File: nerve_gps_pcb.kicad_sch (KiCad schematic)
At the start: 20 parts, among them J1 BF080-16-A-1-L-C, J2 WS2812B, J3 5V GPIO Breakout, U1 SAM-M10Q, U2 TXB0104QPWRQ1

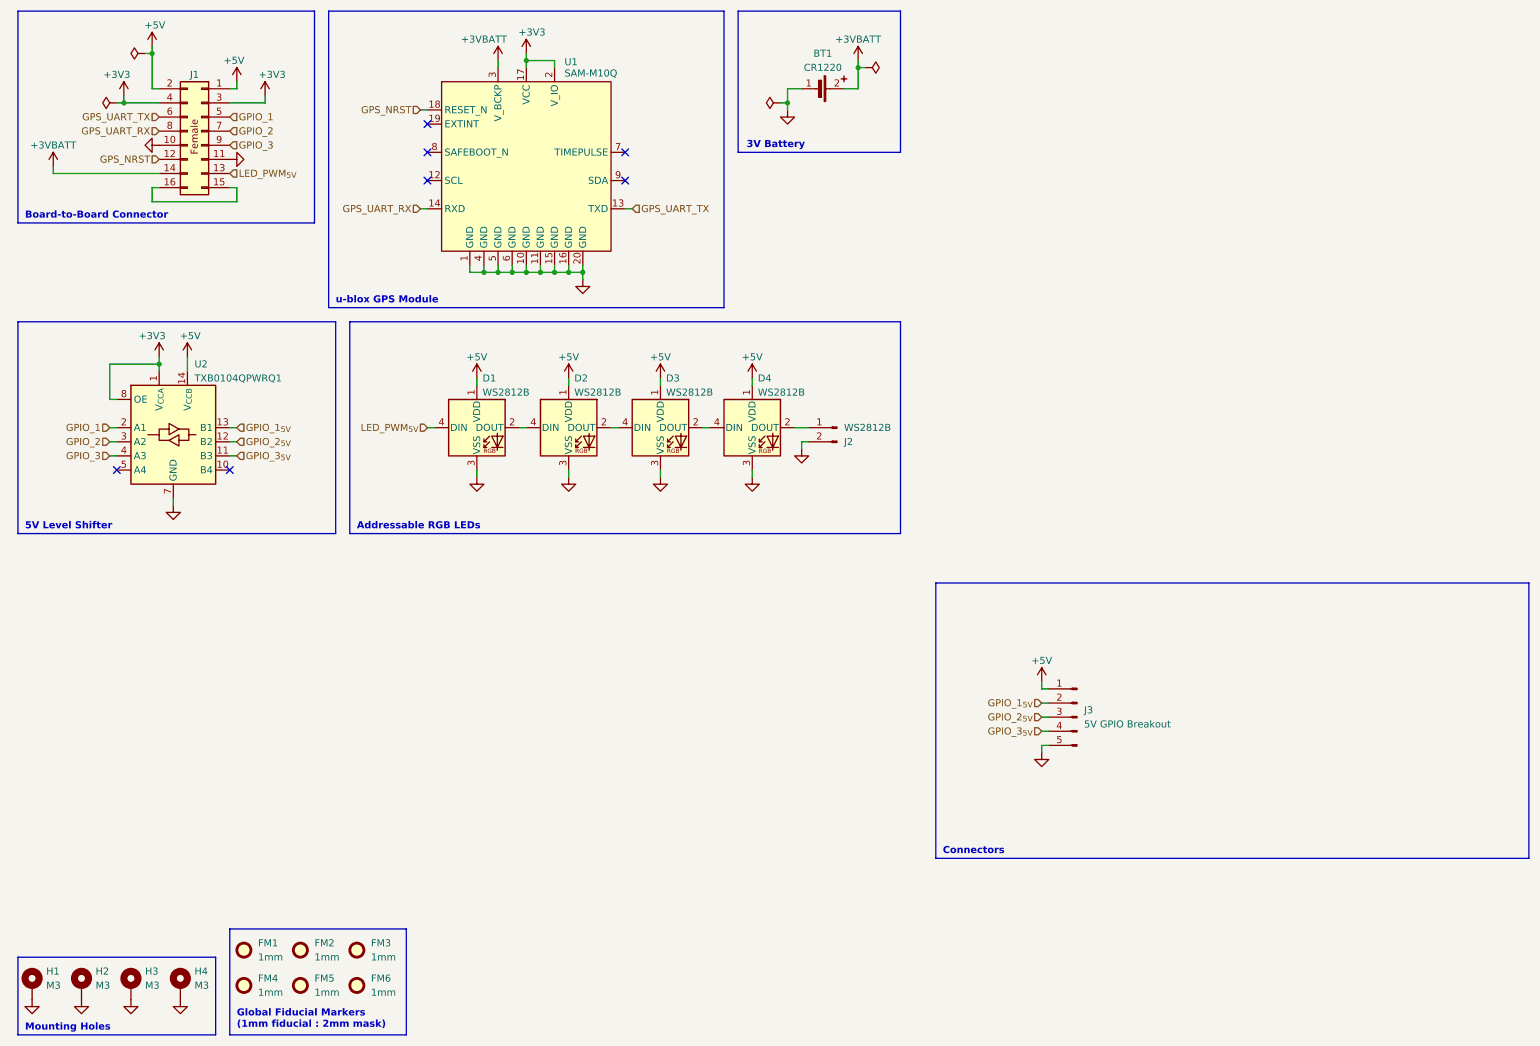
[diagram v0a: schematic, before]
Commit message: Add minor decoupling caps
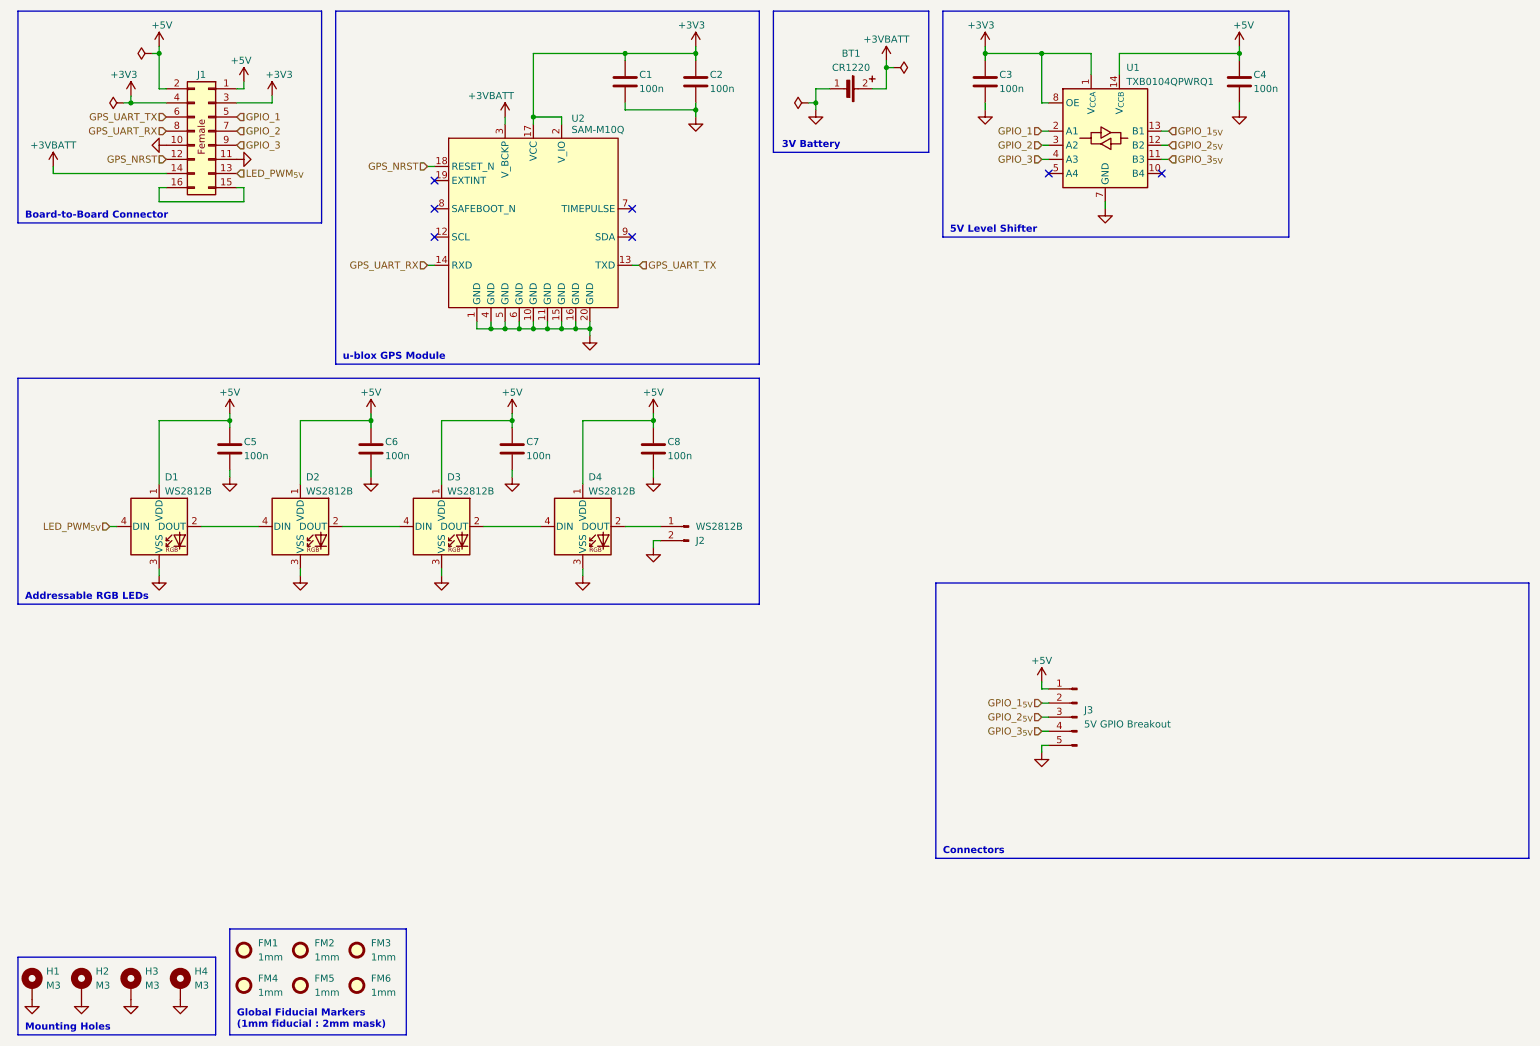
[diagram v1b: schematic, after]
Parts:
- added C1, C2, C3, C4, C5, C6, C7, C8: 100n, Capacitor_SMD:C_0603_1608Metric, symbol Device:C
- renumbered U2 to U1, U1 to U2
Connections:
- net +3V3: now also C1.1, C2.1, C3.1
- net +5V: now also C4.1, C5.1, C6.1, C7.1, C8.1
- net GND: now also C1.2, C2.2, C3.2, C4.2, C5.2, C6.2, C7.2, C8.2
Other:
- moved on the sheet: BT1, D1, D2, D3, D4, J1, J2, U1, U2

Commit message: Add CR1220 reverse polarity schottky diode
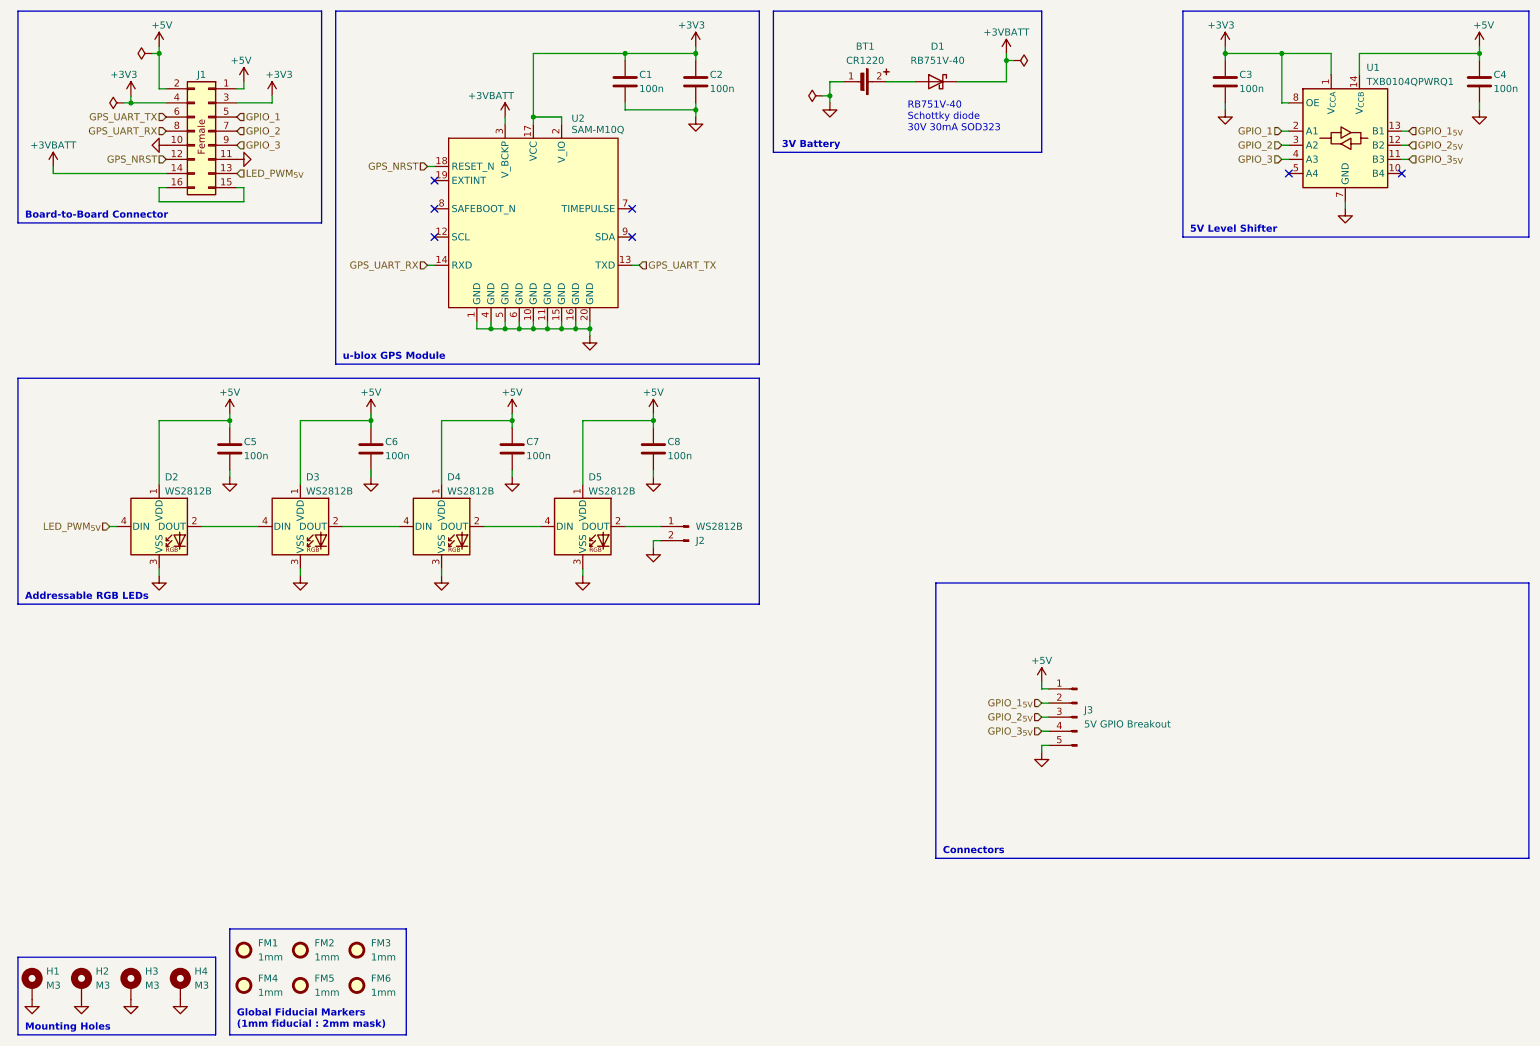
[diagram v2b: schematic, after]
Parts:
- added D1: RB751V-40, Diode_SMD:D_SOD-323, symbol Device:D_Schottky
- renumbered D1 to D2, D2 to D3, D3 to D4, D4 to D5
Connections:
- net +3VBATT: now also D1.1 (K); no longer BT1.2
- new net: BT1.2, D1.2 (A)
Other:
- note added: "RB751V-40 Schottky diode 30V 30mA SOD323"
- moved on the sheet: BT1, C3, C4, U1

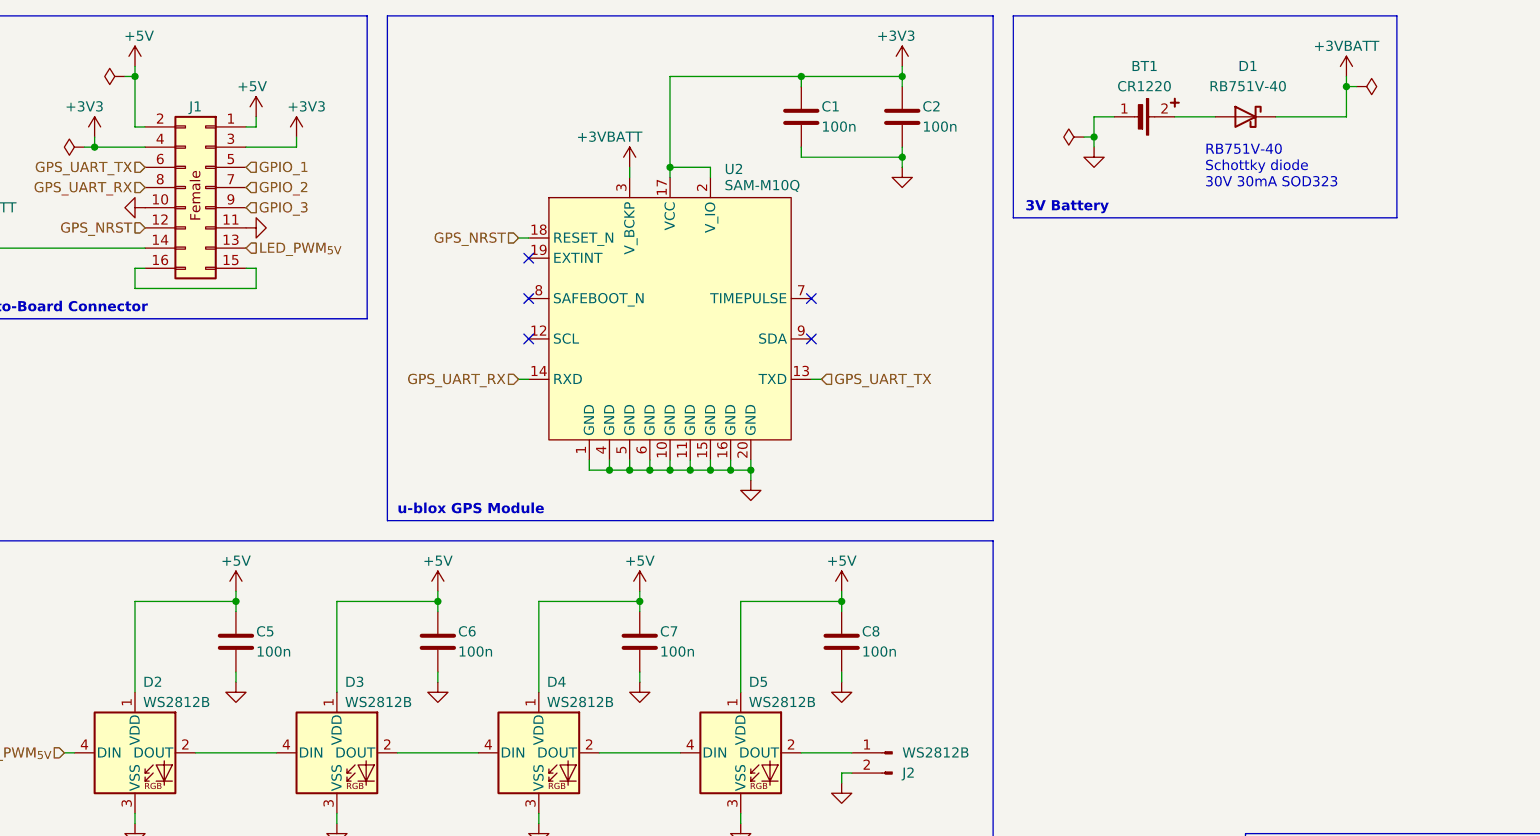
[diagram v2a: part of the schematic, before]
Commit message: Remove CR1220 schottky diode
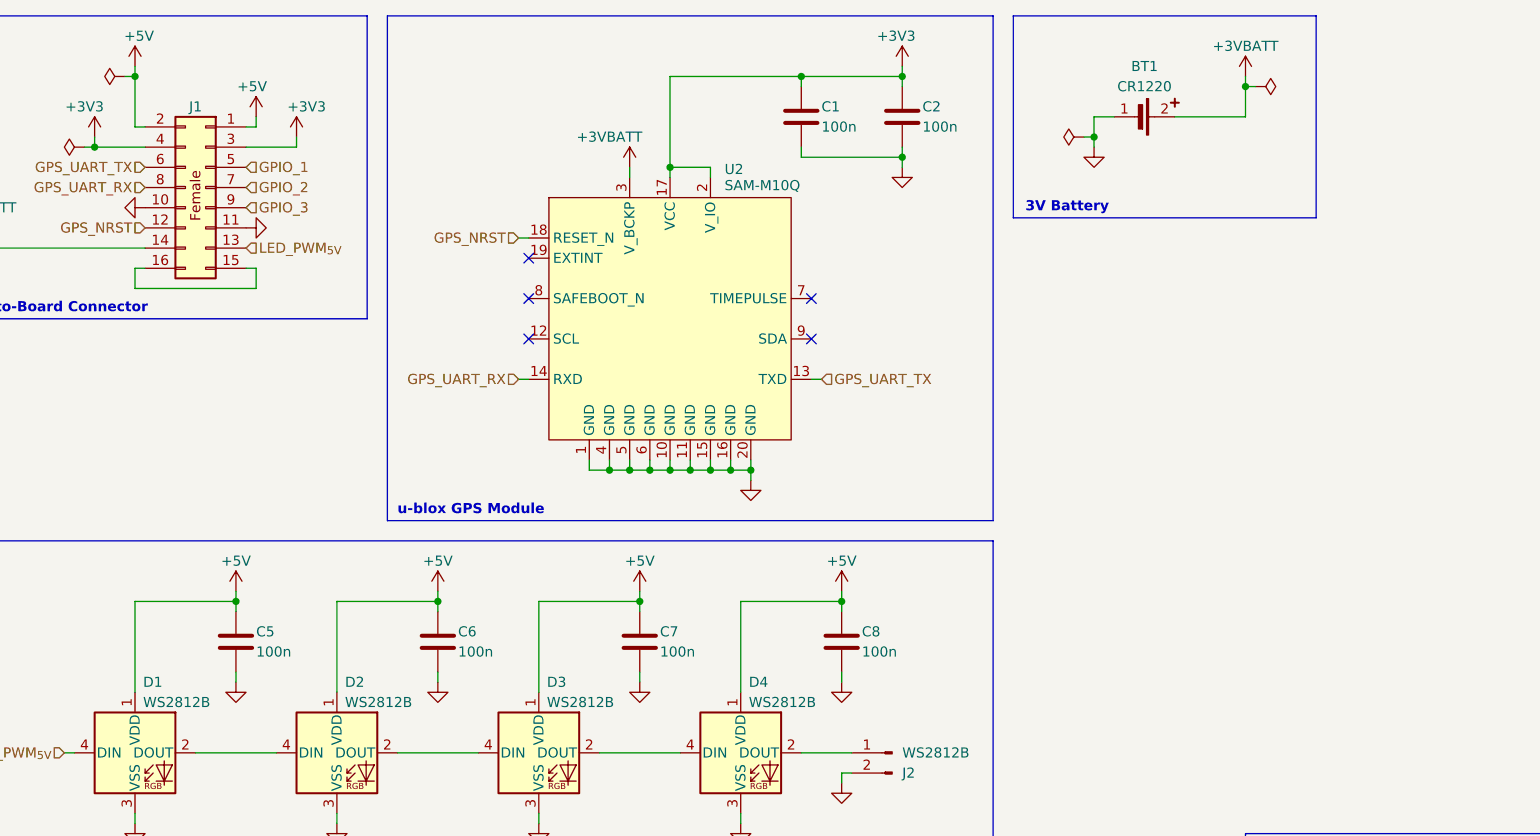
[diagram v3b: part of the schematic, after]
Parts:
- removed D1: RB751V-40, Diode_SMD:D_SOD-323, symbol Device:D_Schottky
- renumbered D2 to D1, D3 to D2, D4 to D3, D5 to D4
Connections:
- net +3VBATT: now also BT1.2
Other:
- note removed: "RB751V-40 Schottky diode 30V 30mA SOD323"
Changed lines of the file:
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@@
 	(rectangle
 		(start 148.59 12.7)
-		(end 196.85 38.1)
+		(end 186.69 38.1)
 		(stroke
 			(width 0)
@@
 		)
 	)
-	(text "RB751V-40\nSchottky diode\n30V 30mA SOD323"
-		(exclude_from_sim no)
-		(at 172.72 31.75 0)
-		(effects
-			(font
-				(size 1.27 1.27)
-				(thickness 0.1588)
-			)
-			(justify left)
-		)
-	)
 	(junction
 		(at 115.57 69.85)
@@
 	)
 	(junction
-		(at 190.5 21.59)
+		(at 177.8 21.59)
 		(diameter 0)
 		(color 0 0 0 0)
@@
 	(wire
 		(pts
-			(xy 190.5 20.32) (xy 190.5 21.59)
+			(xy 177.8 20.32) (xy 177.8 21.59)
 		)
 		(stroke
@@
 	(wire
 		(pts
-			(xy 181.61 25.4) (xy 190.5 25.4)
-		)
-		(stroke
-			(width 0)
-			(type default)
-		)
-	)
-	(wire
-		(pts
 			(xy 114.3 113.03) (xy 114.3 114.3)
 		)
@@
 	(wire
 		(pts
-			(xy 190.5 21.59) (xy 191.77 21.59)
+			(xy 177.8 21.59) (xy 179.07 21.59)
 		)
 		(stroke
@@
 	(wire
 		(pts
-			(xy 168.91 25.4) (xy 173.99 25.4)
+			(xy 168.91 25.4) (xy 177.8 25.4)
 		)
 		(stroke
@@
 	(wire
 		(pts
-			(xy 190.5 21.59) (xy 190.5 25.4)
+			(xy 177.8 21.59) (xy 177.8 25.4)
 		)
 		(stroke
@@
 		(on_board yes)
 		(dnp no)
-		(property "Reference" "D5"
+		(property "Reference" "D4"
 			(at 115.316 96.52 0)
 			(effects
@@
 			(project "nerve_gps_pcb"
 				(path "/c0277862-b3f2-4e0e-986f-34702f0543f0"
-					(reference "D5")
+					(reference "D4")
 					(unit 1)
 				)
@@
 	)
 	(symbol
-		(lib_id "Device:D_Schottky")
-		(at 177.8 25.4 0)
-		(mirror y)
-		(unit 1)
-		(exclude_from_sim no)
-		(in_bom yes)
-		(on_board yes)
-		(dnp no)
-		(property "Reference" "D1"
-			(at 178.1175 19.05 0)
-			(effects
-				(font
-					(size 1.27 1.27)
-				)
-			)
-		)
-		(property "Value" "RB751V-40"
-			(at 178.1175 21.59 0)
-			(effects
-				(font
-					(size 1.27 1.27)
-				)
-			)
-		)
-		(property "Footprint" "Diode_SMD:D_SOD-323"
-			(at 177.8 25.4 0)
-			(effects
-				(font
-					(size 1.27 1.27)
-				)
-				(hide yes)
-			)
-		)
-		(property "Datasheet" "~"
-			(at 177.8 25.4 0)
-			(effects
-				(font
-					(size 1.27 1.27)
-				)
-				(hide yes)
-			)
-		)
-		(property "Description" "Schottky diode"
-			(at 177.8 25.4 0)
-			(effects
-				(font
-					(size 1.27 1.27)
-				)
-				(hide yes)
-			)
-		)
-		(pin "1"
-		)
-		(pin "2"
-		)
-		(instances
-			(project "nerve_gps_pcb"
-				(path "/c0277862-b3f2-4e0e-986f-34702f0543f0"
-					(reference "D1")
-					(unit 1)
-				)
-			)
-		)
-	)
-	(symbol
 		(lib_id "power:GND")
 		(at 15.24 190.5 0)
@@
 	(symbol
 		(lib_id "power:+3V3")
-		(at 190.5 20.32 0)
+		(at 177.8 20.32 0)
 		(unit 1)
 		(exclude_from_sim no)
@@
 		(dnp no)
 		(property "Reference" "#PWR05"
-			(at 190.5 24.13 0)
+			(at 177.8 24.13 0)
 			(effects
 				(font
@@
 		)
 		(property "Value" "+3VBATT"
-			(at 190.5 16.51 0)
+			(at 177.8 16.51 0)
 			(effects
 				(font
@@
 		)
 		(property "Footprint" ""
-			(at 190.5 20.32 0)
+			(at 177.8 20.32 0)
 			(effects
 				(font
@@
 		)
 		(property "Datasheet" ""
-			(at 190.5 20.32 0)
+			(at 177.8 20.32 0)
 			(effects
 				(font
@@
 		)
 		(property "Description" "Power symbol creates a global label with name \"+3V3\""
-			(at 190.5 20.32 0)
+			(at 177.8 20.32 0)
 			(effects
 				(font
@@
 		(on_board yes)
 		(dnp no)
-		(property "Reference" "D4"
+		(property "Reference" "D3"
 			(at 89.916 96.52 0)
 			(effects
@@
 			(project "nerve_gps_pcb"
 				(path "/c0277862-b3f2-4e0e-986f-34702f0543f0"
-					(reference "D4")
+					(reference "D3")
 					(unit 1)
 				)
@@
 		(on_board yes)
 		(dnp no)
-		(property "Reference" "D3"
+		(property "Reference" "D2"
 			(at 64.516 96.52 0)
 			(effects
@@
 			(project "nerve_gps_pcb"
 				(path "/c0277862-b3f2-4e0e-986f-34702f0543f0"
-					(reference "D3")
+					(reference "D2")
 					(unit 1)
 				)
@@
 	(symbol
 		(lib_id "power:PWR_FLAG")
-		(at 191.77 21.59 270)
+		(at 179.07 21.59 270)
 		(unit 1)
 		(exclude_from_sim no)
@@
 		(fields_autoplaced yes)
 		(property "Reference" "#FLG02"
-			(at 193.675 21.59 0)
+			(at 180.975 21.59 0)
 			(effects
 				(font
@@
 		)
 		(property "Value" "PWR_FLAG"
-			(at 196.85 21.59 0)
+			(at 184.15 21.59 0)
 			(effects
 				(font
@@
 		)
 		(property "Footprint" ""
-			(at 191.77 21.59 0)
+			(at 179.07 21.59 0)
 			(effects
 				(font
@@
 		)
 		(property "Datasheet" "~"
-			(at 191.77 21.59 0)
+			(at 179.07 21.59 0)
 			(effects
 				(font
@@
 		)
 		(property "Description" "Special symbol for telling ERC where power comes from"
-			(at 191.77 21.59 0)
+			(at 179.07 21.59 0)
 			(effects
 				(font
@@
 		(on_board yes)
 		(dnp no)
-		(property "Reference" "D2"
+		(property "Reference" "D1"
 			(at 39.116 96.52 0)
 			(effects
@@
 			(project "nerve_gps_pcb"
 				(path "/c0277862-b3f2-4e0e-986f-34702f0543f0"
-					(reference "D2")
+					(reference "D1")
 					(unit 1)
 				)
